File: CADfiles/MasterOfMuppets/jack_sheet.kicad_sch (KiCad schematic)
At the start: 8 parts

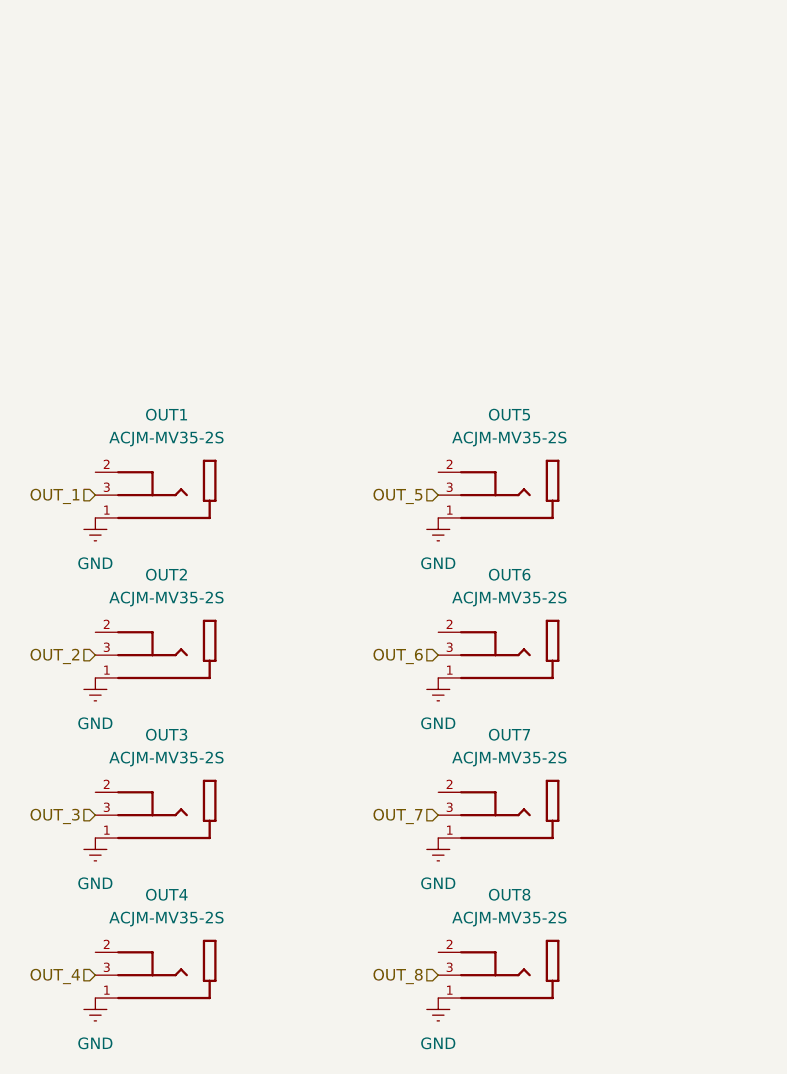
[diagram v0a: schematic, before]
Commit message: Preps for PCB Layout
- PCB Reset;
- Footprint assignment - opting for SMD over THT. I got tired of this much soldering;
- Fixing path for teensy.kicad_sym
- Changed symbols of the 3.5mm jack connector to the usual one seen in Eurorack (thanks for the symbols, 4ms!) ;
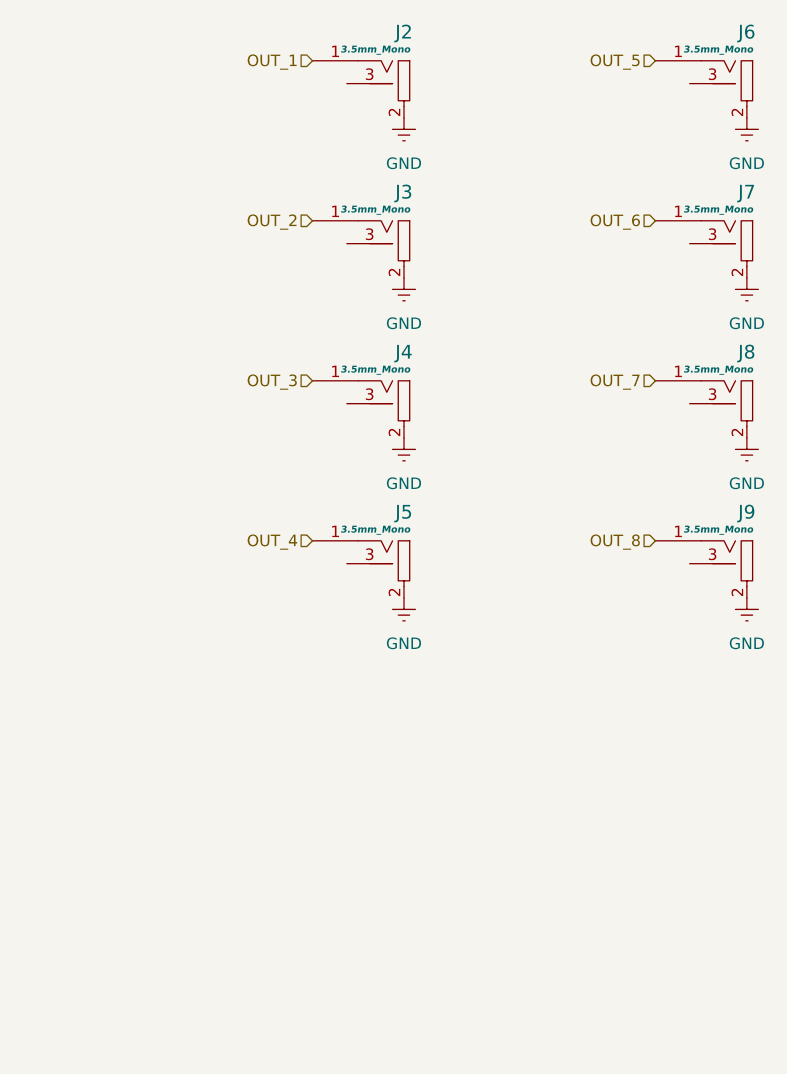
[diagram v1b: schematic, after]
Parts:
- J2: renamed from OUT1; value ACJM-MV35-2S -> 3.5mm_Mono_Switched_SymSmall_0.05; footprint PCM_4ms_Jack:ACJM-MV35-2S_Mono_Vert_Switch -> 4ms_Jack:EighthInch_PJ398SM; symbol ACJM-MV35-2S:ACJM-MV35-2S -> PCM_4ms_Jack:3.5mm_Mono_Switched_SymSmall_0.05; Display (none) -> 3.5mm_Mono; Manufacturer (none) -> Wenzhou QingPu Electronics Co; Part Number (none) -> WQP-WQP518MA; Specifications (none) -> Audio 3.5mm Jack, mono, switched, PC-pin Vertical
- J3: renamed from OUT2; value ACJM-MV35-2S -> 3.5mm_Mono_Switched_SymSmall_0.05; footprint PCM_4ms_Jack:ACJM-MV35-2S_Mono_Vert_Switch -> 4ms_Jack:EighthInch_PJ398SM; symbol ACJM-MV35-2S:ACJM-MV35-2S -> PCM_4ms_Jack:3.5mm_Mono_Switched_SymSmall_0.05; Display (none) -> 3.5mm_Mono; Manufacturer (none) -> Wenzhou QingPu Electronics Co; Part Number (none) -> WQP-WQP518MA; Specifications (none) -> Audio 3.5mm Jack, mono, switched, PC-pin Vertical
- J4: renamed from OUT3; value ACJM-MV35-2S -> 3.5mm_Mono_Switched_SymSmall_0.05; footprint PCM_4ms_Jack:ACJM-MV35-2S_Mono_Vert_Switch -> 4ms_Jack:EighthInch_PJ398SM; symbol ACJM-MV35-2S:ACJM-MV35-2S -> PCM_4ms_Jack:3.5mm_Mono_Switched_SymSmall_0.05; Display (none) -> 3.5mm_Mono; Manufacturer (none) -> Wenzhou QingPu Electronics Co; Part Number (none) -> WQP-WQP518MA; Specifications (none) -> Audio 3.5mm Jack, mono, switched, PC-pin Vertical
- J5: renamed from OUT4; value ACJM-MV35-2S -> 3.5mm_Mono_Switched_SymSmall_0.05; footprint PCM_4ms_Jack:ACJM-MV35-2S_Mono_Vert_Switch -> 4ms_Jack:EighthInch_PJ398SM; symbol ACJM-MV35-2S:ACJM-MV35-2S -> PCM_4ms_Jack:3.5mm_Mono_Switched_SymSmall_0.05; Display (none) -> 3.5mm_Mono; Manufacturer (none) -> Wenzhou QingPu Electronics Co; Part Number (none) -> WQP-WQP518MA; Specifications (none) -> Audio 3.5mm Jack, mono, switched, PC-pin Vertical
- J6: renamed from OUT5; value ACJM-MV35-2S -> 3.5mm_Mono_Switched_SymSmall_0.05; footprint PCM_4ms_Jack:ACJM-MV35-2S_Mono_Vert_Switch -> 4ms_Jack:EighthInch_PJ398SM; symbol ACJM-MV35-2S:ACJM-MV35-2S -> PCM_4ms_Jack:3.5mm_Mono_Switched_SymSmall_0.05; Display (none) -> 3.5mm_Mono; Manufacturer (none) -> Wenzhou QingPu Electronics Co; Part Number (none) -> WQP-WQP518MA; Specifications (none) -> Audio 3.5mm Jack, mono, switched, PC-pin Vertical
- J7: renamed from OUT6; value ACJM-MV35-2S -> 3.5mm_Mono_Switched_SymSmall_0.05; footprint PCM_4ms_Jack:ACJM-MV35-2S_Mono_Vert_Switch -> 4ms_Jack:EighthInch_PJ398SM; symbol ACJM-MV35-2S:ACJM-MV35-2S -> PCM_4ms_Jack:3.5mm_Mono_Switched_SymSmall_0.05; Display (none) -> 3.5mm_Mono; Manufacturer (none) -> Wenzhou QingPu Electronics Co; Part Number (none) -> WQP-WQP518MA; Specifications (none) -> Audio 3.5mm Jack, mono, switched, PC-pin Vertical
- J8: renamed from OUT7; value ACJM-MV35-2S -> 3.5mm_Mono_Switched_SymSmall_0.05; footprint PCM_4ms_Jack:ACJM-MV35-2S_Mono_Vert_Switch -> 4ms_Jack:EighthInch_PJ398SM; symbol ACJM-MV35-2S:ACJM-MV35-2S -> PCM_4ms_Jack:3.5mm_Mono_Switched_SymSmall_0.05; Display (none) -> 3.5mm_Mono; Manufacturer (none) -> Wenzhou QingPu Electronics Co; Part Number (none) -> WQP-WQP518MA; Specifications (none) -> Audio 3.5mm Jack, mono, switched, PC-pin Vertical
- J9: renamed from OUT8; value ACJM-MV35-2S -> 3.5mm_Mono_Switched_SymSmall_0.05; footprint PCM_4ms_Jack:ACJM-MV35-2S_Mono_Vert_Switch -> 4ms_Jack:EighthInch_PJ398SM; symbol ACJM-MV35-2S:ACJM-MV35-2S -> PCM_4ms_Jack:3.5mm_Mono_Switched_SymSmall_0.05; Display (none) -> 3.5mm_Mono; Manufacturer (none) -> Wenzhou QingPu Electronics Co; Part Number (none) -> WQP-WQP518MA; Specifications (none) -> Audio 3.5mm Jack, mono, switched, PC-pin Vertical
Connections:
- net GND: now also J2.2 (SHEILD), J3.2 (SHEILD), J4.2 (SHEILD), J5.2 (SHEILD), J6.2 (SHEILD), J7.2 (SHEILD), J8.2 (SHEILD), J9.2 (SHEILD); no longer J2.1, J3.1, J4.1, J5.1, J6.1, J7.1, J8.1, J9.1
- net OUT_1: now also J2.1 (SIG); no longer J2.3
- net OUT_2: now also J3.1 (SIG); no longer J3.3
- net OUT_3: now also J4.1 (SIG); no longer J4.3
- net OUT_4: now also J5.1 (SIG); no longer J5.3
- net OUT_5: now also J6.1 (SIG); no longer J6.3
- net OUT_6: now also J7.1 (SIG); no longer J7.3
- net OUT_7: now also J8.1 (SIG); no longer J8.3
- net OUT_8: now also J9.1 (SIG); no longer J9.3

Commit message: PCB Preps
Re-assigned footprints;
Placed all symbols in the middle;
Removed instruction to ignore the PCB in the README.manahmanah;
Added a generic placement recommendation file from Sir. Claude;
Ready to start the design;
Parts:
- J2, J3, J4, J5, J6, J7, J8, J9: footprint 4ms_Jack:EighthInch_PJ398SM -> PCM_4ms_Jack:EighthInch_PJ398SM
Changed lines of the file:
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@@
 			)
 		)
-		(property "Footprint" "4ms_Jack:EighthInch_PJ398SM"
+		(property "Footprint" "PCM_4ms_Jack:EighthInch_PJ398SM"
 			(at 102.87 76.2 0)
 			(effects
@@
 			)
 		)
-		(property "Footprint" "4ms_Jack:EighthInch_PJ398SM"
+		(property "Footprint" "PCM_4ms_Jack:EighthInch_PJ398SM"
 			(at 64.77 40.64 0)
 			(effects
@@
 			)
 		)
-		(property "Footprint" "4ms_Jack:EighthInch_PJ398SM"
+		(property "Footprint" "PCM_4ms_Jack:EighthInch_PJ398SM"
 			(at 64.77 58.42 0)
 			(effects
@@
 			)
 		)
-		(property "Footprint" "4ms_Jack:EighthInch_PJ398SM"
+		(property "Footprint" "PCM_4ms_Jack:EighthInch_PJ398SM"
 			(at 102.87 40.64 0)
 			(effects
@@
 			)
 		)
-		(property "Footprint" "4ms_Jack:EighthInch_PJ398SM"
+		(property "Footprint" "PCM_4ms_Jack:EighthInch_PJ398SM"
 			(at 64.77 93.98 0)
 			(effects
@@
 			)
 		)
-		(property "Footprint" "4ms_Jack:EighthInch_PJ398SM"
+		(property "Footprint" "PCM_4ms_Jack:EighthInch_PJ398SM"
 			(at 102.87 93.98 0)
 			(effects
@@
 			)
 		)
-		(property "Footprint" "4ms_Jack:EighthInch_PJ398SM"
+		(property "Footprint" "PCM_4ms_Jack:EighthInch_PJ398SM"
 			(at 102.87 58.42 0)
 			(effects
@@
 			)
 		)
-		(property "Footprint" "4ms_Jack:EighthInch_PJ398SM"
+		(property "Footprint" "PCM_4ms_Jack:EighthInch_PJ398SM"
 			(at 64.77 76.2 0)
 			(effects
